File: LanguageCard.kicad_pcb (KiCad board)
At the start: 2 copper layers, 100 x 77.5 mm, 29 parts, among them J1 Apple II Expansion Bus, U1 74LS86, U10 74LS06, U2 74LS08, U3 74LS175, U4 74LS32, U5 74LS08, U6 74LS08, U7 ROM F8, U8 6264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

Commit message: support larger SRAMS, minor updates
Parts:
- R1, R2, R3, R4, R5, R6: footprint Resistor_THT:R_Axial_DIN0207_L6.3mm_D2.5mm_P7.62mm_Horizontal -> Resistor_THT:R_Axial_DIN0207_L6.3mm_D2.5mm_P10.16mm_Horizontal
- moved R6 154.9 mm to (114.9, 71.1)
- moved R4 152.4 mm to (108.0, 27.9)
- moved R1 152.4 mm to (45.1, 29.2)
- moved R3 152.4 mm to (97.8, 27.9)
- moved R5 152.4 mm to (118.1, 27.9)
- moved D2 152.4 mm to (104.1, 30.5)
- moved D4 152.4 mm to (124.5, 30.5)
- moved U4 152.4 mm to (85.1, 67.3)
- moved C2 152.4 mm to (67.9, 34.2)
- moved C3 152.4 mm to (33.1, 44.5)
- moved C6 152.4 mm to (103.5, 81.3)
- moved C7 152.4 mm to (69.8, 47.0)
- moved D1 152.4 mm to (51.4, 31.8)
- moved JP1 152.4 mm to (104.2, 87.6)
- moved U2 152.4 mm to (85.1, 52.1)
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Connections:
- U8 pad 1: unconnected-(U8-Pad1) -> +5V
- U9 pad 1: unconnected-(U9-Pad1) -> +5V
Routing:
- net +5V: track 407.0 -> 424.8 mm
- net /~{WE}: track 49.6 -> 51.5 mm
- net Net-(D4-Pad2): track 3.81 -> 5.22 mm
- net Net-(D3-Pad2): track 3.81 -> 5.16 mm
- net Net-(D2-Pad2): track 3.81 -> 5.16 mm
- net /RAMCE: track 135.2 -> 135.7 mm
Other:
- board text added: "R3, R4, R5: Use higher resistance for high-efficiency LEDs, e.g. 3.3K U8 and U9: Any narrow 8KBx8 static RAM can be used. ex: Cy6264, 5C6408, Cy7C185, TC5588 Higher capacities such as the Cy7C199 can be used but only 8K in each socket will be addressable."

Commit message: no, 32kx8 does not work. need two chip selects
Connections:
- U8 pad 1: +5V -> unconnected-(U8-Pad1)
- U9 pad 1: +5V -> unconnected-(U9-Pad1)
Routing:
- net +5V: track 424.8 -> 409.5 mm
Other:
- board text added: "R3, R4, R5: Use higher resistance for high-efficiency LEDs, e.g. 3.3K U8 and U9: Any narrow 8KBx8 static RAM can be used. ex: Cy6264, 5C6408, Cy7C185, TC5588"
- board text removed: "R3, R4, R5: Use higher resistance for high-efficiency LEDs, e.g. 3.3K U8 and U9: Any narrow 8KBx8 static RAM can be used. ex: Cy6264, 5C6408, Cy7C185, TC5588 Higher capacities such as the Cy7C199 can be used but only 8K in each socket will be addressable."

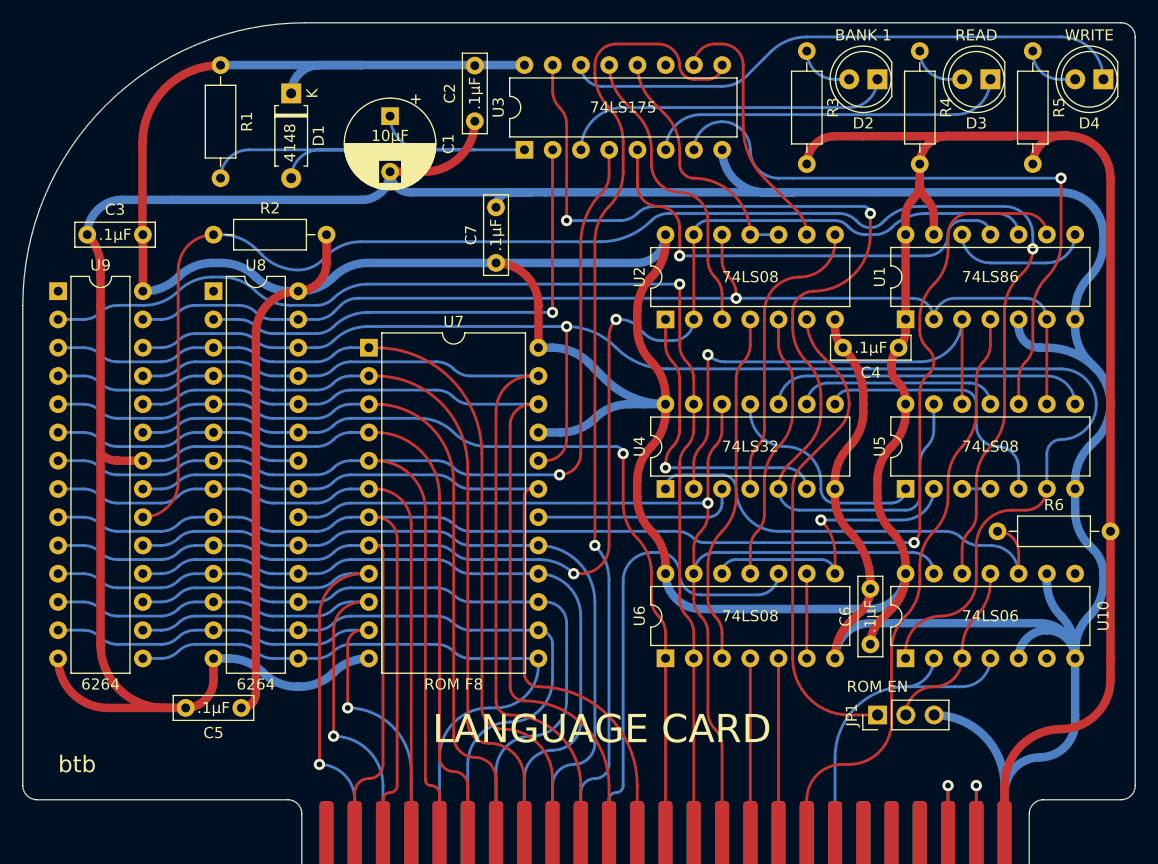
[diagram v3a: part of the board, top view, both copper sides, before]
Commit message: add teardrops
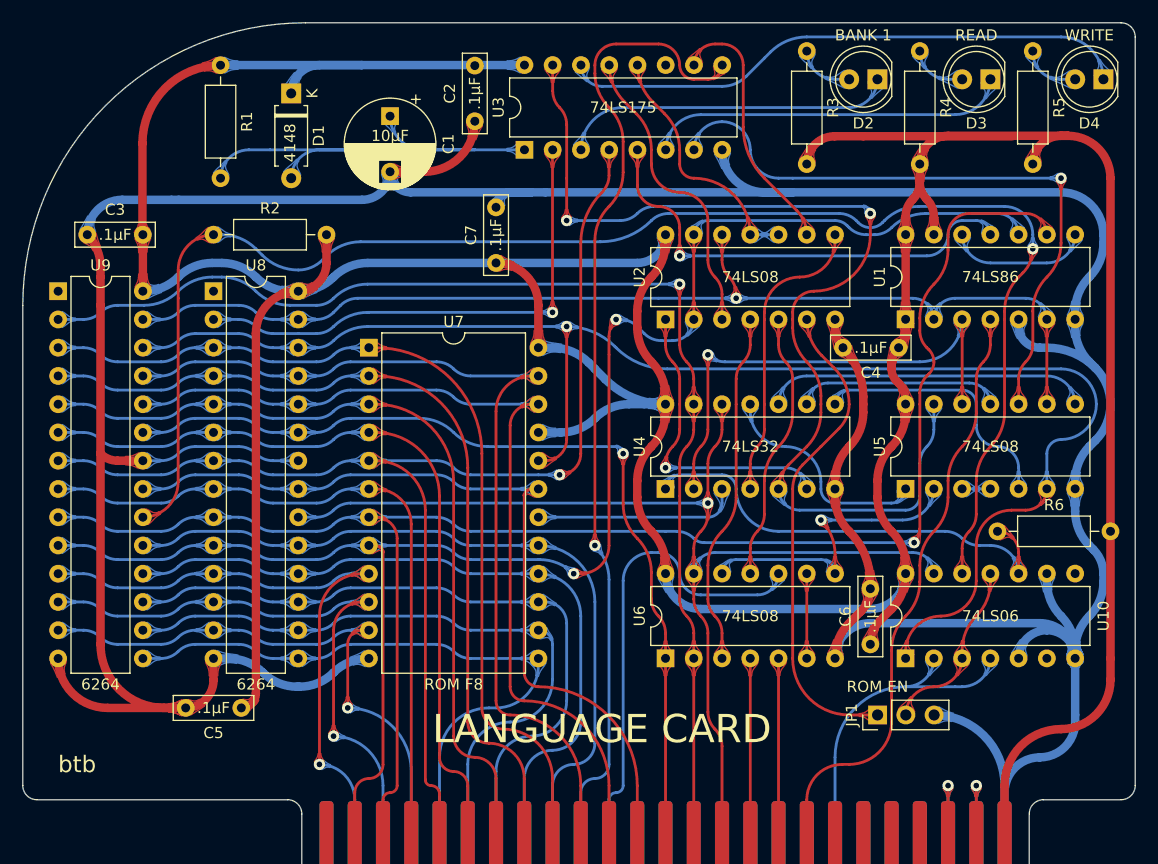
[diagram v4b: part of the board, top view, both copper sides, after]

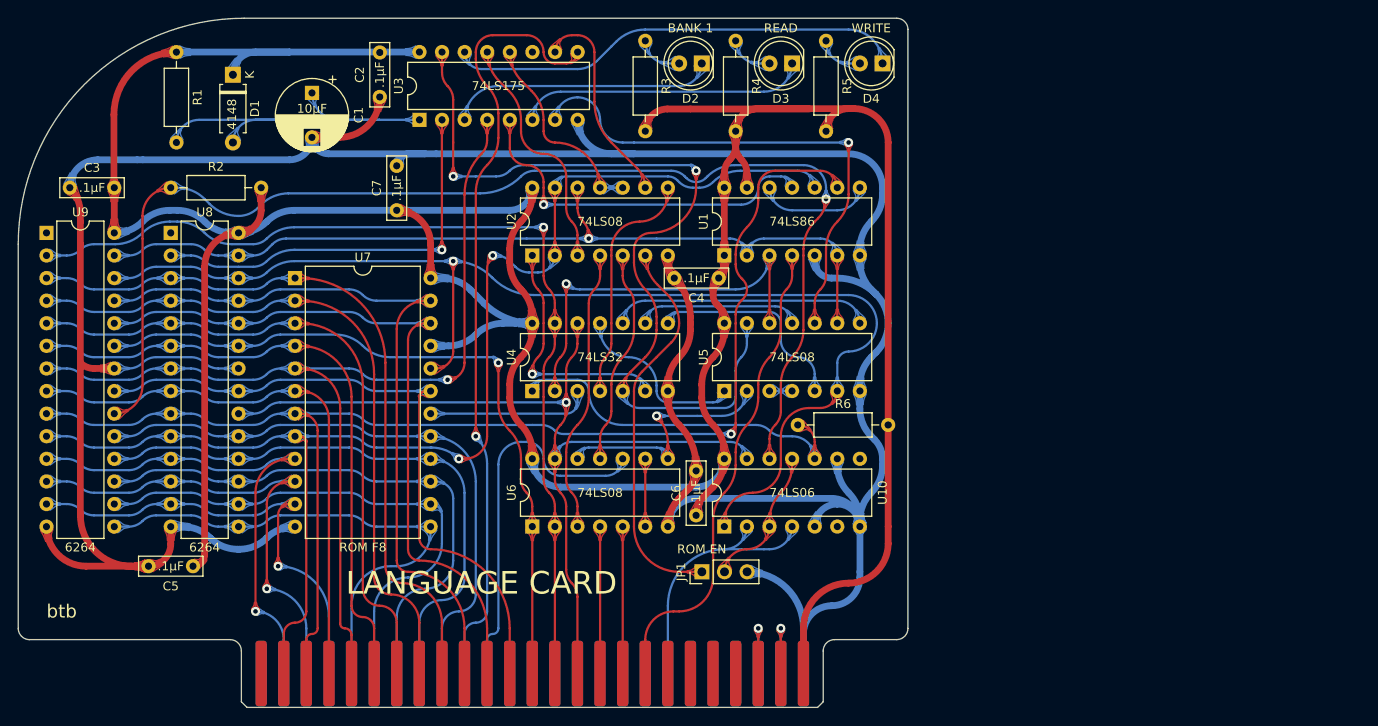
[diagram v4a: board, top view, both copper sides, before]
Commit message: fix up silkscreens and fabs
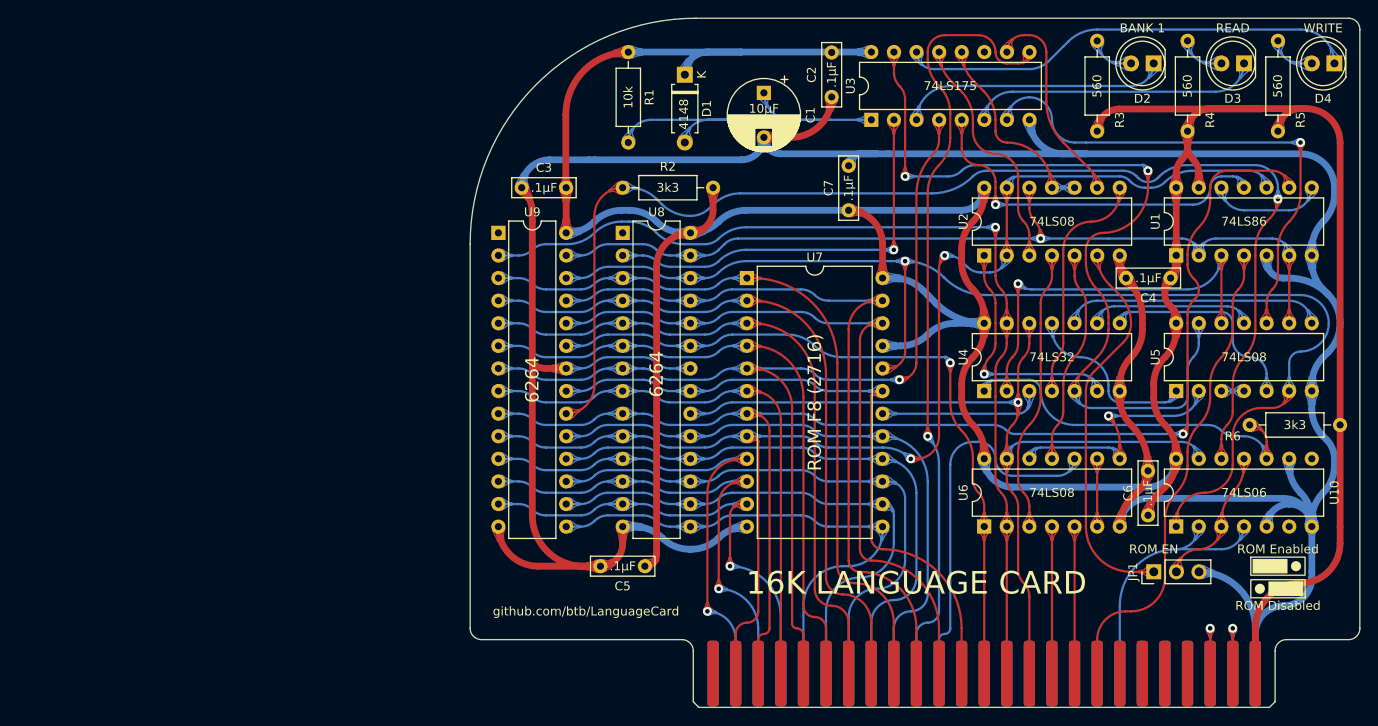
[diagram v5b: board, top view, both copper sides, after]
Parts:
- added REF**: ROM Disabled, MySymbol:Jumper_SilkScreen, F.Cu at (168.9, 89.5)
- added REF**: ROM Enabled, MySymbol:Jumper_SilkScreen, F.Cu at (168.9, 87.0)
- U7: value ROM F8 -> ROM F8 (2716)
- moved C2 50.8 mm to (118.7, 34.2)
- moved C6 50.8 mm to (154.3, 81.3)
- moved C7 50.8 mm to (120.7, 47.0)
- moved JP1 50.8 mm to (155.0, 87.6)
- moved R6 50.8 mm to (165.7, 71.1)
- moved C3 50.8 mm to (83.9, 44.5)
- moved R1 50.8 mm to (95.9, 29.2)
- moved C1 50.8 mm to (111.1, 33.8)
- moved C4 50.8 mm to (156.8, 54.6)
- moved C5 50.8 mm to (97.8, 87.0)
- moved D1 50.8 mm to (102.2, 31.8)
- moved D2 50.8 mm to (154.9, 30.5)
- moved D3 50.8 mm to (165.1, 30.5)
- moved D4 50.8 mm to (175.3, 30.5)
- moved J1 50.8 mm to (119.4, 94.1)
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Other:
- board text added: "16K LANGUAGE CARD"
- board text added: "R3, R4, R5: Use higher resistance for high-efficiency LEDs, e.g. 3.3K"
- board text added: "U8 and U9: Any narrow 8KBx8 static RAM can be used. ex: 5C6408, Cy7C185, TC5588"
- board text added: "github.com/btb/LanguageCard"
- board text removed: "LANGUAGE CARD"
- board text removed: "R3, R4, R5: Use higher resistance for high-efficiency LEDs, e.g. 3.3K U8 and U9: Any narrow 8KBx8 static RAM can be used. ex: Cy6264, 5C6408, Cy7C185, TC5588"
- board text removed: "btb"
